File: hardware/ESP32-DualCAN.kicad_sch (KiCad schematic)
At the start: 32 parts, among them J1 Molex 70553 6p, J2 Conn_01x10_Socket, J3 Conn_01x10_Socket, J4 holes, J5 pads, J6 holes, J7 pads, U1 LV2862Y, U2 ESP32-C6-SuperMini, U3 TCAN1044AV, U4 TCAN1044AV, U5 ESP32-C6-Zero, U6 ESP32-C6-SuperMini

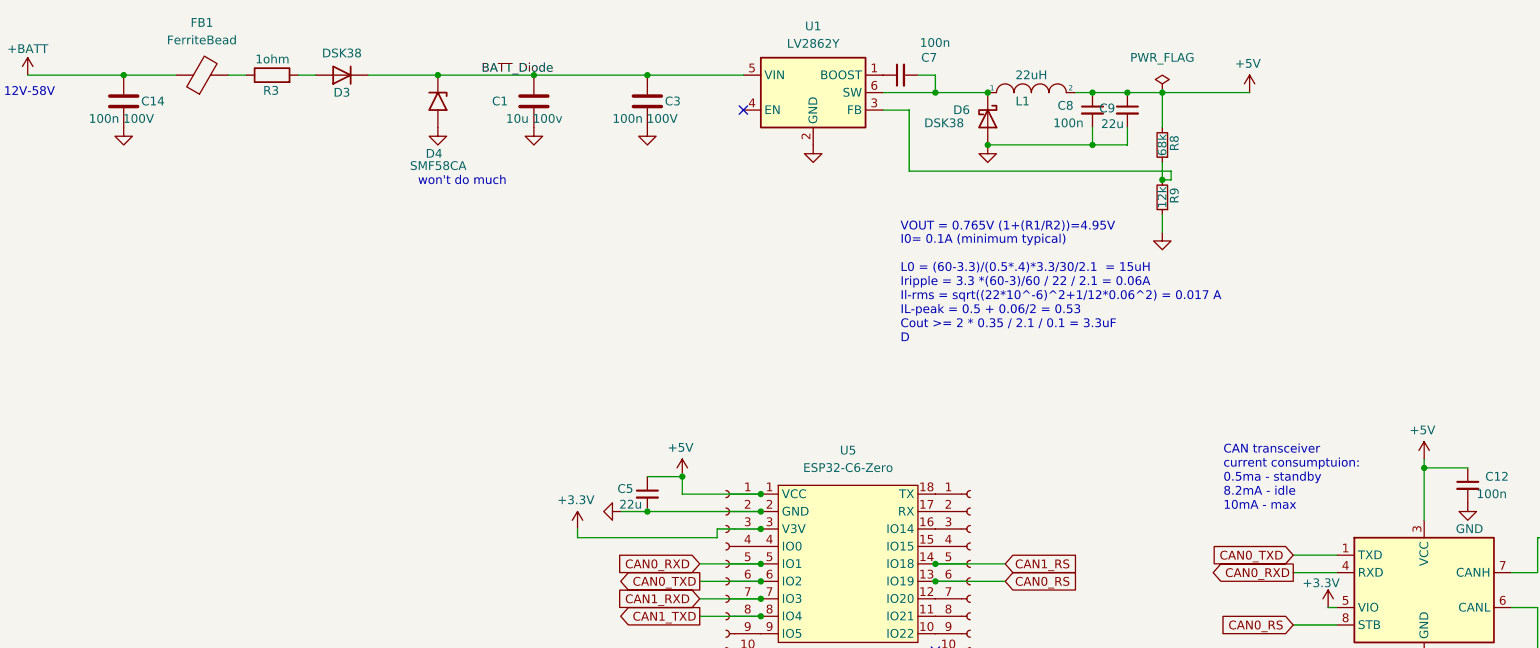
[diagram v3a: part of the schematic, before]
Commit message: DNP input filtering.  Changed vout resistors
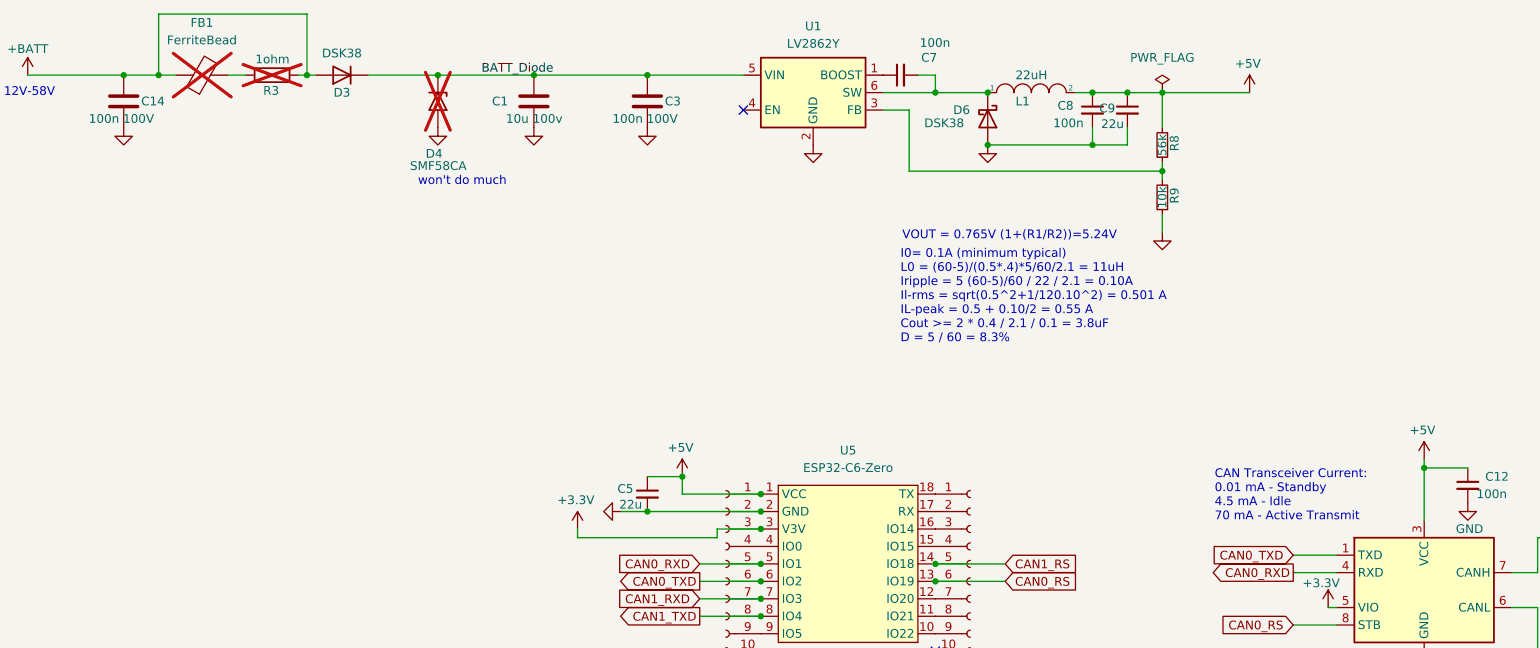
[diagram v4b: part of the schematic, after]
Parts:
- D4, FB1, R3: now not fitted
- J1: LCSC C24361 -> C704582
- R8: value 68k -> 56k; LCSC C36871 -> C25744
- R9: value 12k -> 10k; LCSC C25752 -> C25744
- U1: Alternative LMR51606YF -> LV2862Y, LMR16006Y, LMR51606YF
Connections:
- net +BATT: now also D3.2 (A), R3.2
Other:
- note added: "CAN Transceiver Current: 0.01 mA - Standby 4.5 mA - Idle 70 mA - Active Transmit"
- note added: "I0= 0.1A (minimum typical) L0 = (60-5)/(0.5*.4)*5/60/2.1 = 11uH Iripple = 5 (60-5)/60 / 22 / 2.1 = 0.10A Il-rms = sqrt(0.5^2+1/120.10^2) = 0.501 A IL-peak = 0.5 + 0.10/2 = 0.55 A Cout >= 2 * 0.4 / 2.1 / 0.1 = 3.8uF D = 5 / 60 = 8.3%"
- note added: "VOUT = 0.765V (1+(R1/R2))=5.24V"
- note removed: "CAN transceiver current consumptuion: 0.5ma - standby 8.2mA - idle 10mA - max"
- note removed: "I0= 0.1A (minimum typical) L0 = (60-3.3)/(0.5*.4)*3.3/30/2.1 = 15uH Iripple = 3.3 *(60-3)/60 / 22 / 2.1 = 0.06A Il-rms = sqrt((22*10^-6)^2+1/12*0.06^2) = 0.017 A IL-peak = 0.5 + 0.06/2 = 0.53 Cout >= 2 * 0.35 / 2.1 / 0.1 = 3.3uF D"
- note removed: "VOUT = 0.765V (1+(R1/R2))=4.95V"
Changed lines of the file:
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@@
 		)
 	)
-	(text "CAN transceiver\ncurrent consumptuion:\n0.5ma - standby\n8.2mA - idle\n10mA - max\n"
+	(text "CAN Transceiver Current:\n0.01 mA - Standby\n4.5 mA - Idle\n70 mA - Active Transmit\n"
 		(exclude_from_sim no)
-		(at 199.39 87.63 0)
+		(at 198.12 89.154 0)
 		(effects
 			(font
@@
 		)
 	)
-	(text "VOUT = 0.765V (1+(R1/R2))=4.95V"
+	(text "VOUT = 0.765V (1+(R1/R2))=5.24V"
 		(exclude_from_sim no)
-		(at 152.4 46.99 0)
+		(at 152.654 48.26 0)
 		(effects
 			(font
@@
 		)
 	)
-	(text "I0= 0.1A (minimum typical)\n\nL0 = (60-3.3)/(0.5*.4)*3.3/30/2.1  = 15uH\nIripple = 3.3 *(60-3)/60 / 22 / 2.1 = 0.06A\nIl-rms = sqrt((22*10^-6)^2+1/12*0.06^2) = 0.017 A\nIL-peak = 0.5 + 0.06/2 = 0.53\nCout >= 2 * 0.35 / 2.1 / 0.1 = 3.3uF\nD"
+	(text "I0= 0.1A (minimum typical)\nL0 = (60-5)/(0.5*.4)*5/60/2.1 = 11uH\nIripple = 5 (60-5)/60 / 22 / 2.1 = 0.10A\nIl-rms = sqrt(0.5^2+1/120.10^2) = 0.501 A\nIL-peak = 0.5 + 0.10/2 = 0.55 A\nCout >= 2 * 0.4 / 2.1 / 0.1 = 3.8uF\nD = 5 / 60 = 8.3%"
 		(exclude_from_sim no)
 		(at 152.4 63.246 0)
@@
 	)
 	(junction
-		(at 190.5 39.37)
-		(diameter 0)
-		(color 0 0 0 0)
-	)
-	(junction
 		(at 73.66 179.07)
 		(diameter 0)
@@
 	)
 	(junction
+		(at 66.04 24.13)
+		(diameter 0)
+		(color 0 0 0 0)
+	)
+	(junction
 		(at 157.48 95.25)
 		(diameter 0)
@@
 	)
 	(junction
+		(at 44.45 24.13)
+		(diameter 0)
+		(color 0 0 0 0)
+	)
+	(junction
 		(at 256.54 91.44)
 		(diameter 0)
@@
 	)
 	(junction
+		(at 190.5 38.1)
+		(diameter 0)
+		(color 0 0 0 0)
+	)
+	(junction
 		(at 73.66 181.61)
 		(diameter 0)
@@
 	(wire
 		(pts
-			(xy 54.61 24.13) (xy 57.15 24.13)
+			(xy 99.06 24.13) (xy 115.57 24.13)
 		)
 		(stroke
@@
 	(wire
 		(pts
-			(xy 99.06 24.13) (xy 115.57 24.13)
+			(xy 49.53 184.15) (xy 50.8 184.15)
 		)
 		(stroke
@@
 	(wire
 		(pts
-			(xy 49.53 184.15) (xy 50.8 184.15)
+			(xy 228.6 81.28) (xy 228.6 88.9)
 		)
 		(stroke
@@
 	(wire
 		(pts
-			(xy 228.6 81.28) (xy 228.6 88.9)
+			(xy 157.48 24.13) (xy 157.48 26.67)
 		)
 		(stroke
@@
 	(wire
 		(pts
-			(xy 157.48 24.13) (xy 157.48 26.67)
+			(xy 200.66 254) (xy 209.55 254)
 		)
 		(stroke
@@
 	(wire
 		(pts
-			(xy 200.66 254) (xy 209.55 254)
+			(xy 105.41 91.44) (xy 125.73 91.44)
 		)
 		(stroke
@@
 	(wire
 		(pts
-			(xy 105.41 91.44) (xy 125.73 91.44)
+			(xy 156.21 254) (xy 147.32 254)
 		)
 		(stroke
@@
 	(wire
 		(pts
-			(xy 156.21 254) (xy 147.32 254)
+			(xy 190.5 38.1) (xy 190.5 39.37)
 		)
 		(stroke
@@
 	(wire
 		(pts
-			(xy 204.47 241.3) (xy 209.55 241.3)
+			(xy 44.45 15.24) (xy 66.04 15.24)
 		)
 		(stroke
@@
 	(wire
 		(pts
-			(xy 123.19 102.87) (xy 132.08 102.87)
+			(xy 204.47 241.3) (xy 209.55 241.3)
 		)
 		(stroke
@@
 	(wire
 		(pts
-			(xy 228.6 110.49) (xy 228.6 109.22)
+			(xy 123.19 102.87) (xy 132.08 102.87)
 		)
 		(stroke
@@
 	(wire
 		(pts
-			(xy 156.21 251.46) (xy 147.32 251.46)
+			(xy 228.6 110.49) (xy 228.6 109.22)
 		)
 		(stroke
@@
 	(wire
 		(pts
-			(xy 121.92 107.95) (xy 132.08 107.95)
+			(xy 156.21 251.46) (xy 147.32 251.46)
 		)
 		(stroke
@@
 	(wire
 		(pts
-			(xy 191.77 38.1) (xy 191.77 39.37)
+			(xy 121.92 107.95) (xy 132.08 107.95)
 		)
 		(stroke
@@
 	(wire
 		(pts
-			(xy 123.19 95.25) (xy 132.08 95.25)
+			(xy 44.45 15.24) (xy 44.45 24.13)
 		)
 		(stroke
@@
 	(wire
 		(pts
-			(xy 180.34 34.29) (xy 185.42 34.29)
+			(xy 123.19 95.25) (xy 132.08 95.25)
 		)
 		(stroke
@@
 	(wire
 		(pts
-			(xy 209.55 135.89) (xy 215.9 135.89)
+			(xy 180.34 34.29) (xy 185.42 34.29)
 		)
 		(stroke
@@
 	(wire
 		(pts
-			(xy 242.57 133.35) (xy 242.57 138.43)
+			(xy 209.55 135.89) (xy 215.9 135.89)
 		)
 		(stroke
@@
 	(wire
 		(pts
-			(xy 64.77 24.13) (xy 67.31 24.13)
+			(xy 242.57 133.35) (xy 242.57 138.43)
 		)
 		(stroke
@@
 	(wire
 		(pts
-			(xy 190.5 26.67) (xy 203.2 26.67)
+			(xy 64.77 24.13) (xy 66.04 24.13)
 		)
 		(stroke
@@
 	(wire
 		(pts
-			(xy 242.57 151.13) (xy 254 151.13)
+			(xy 190.5 26.67) (xy 203.2 26.67)
 		)
 		(stroke
@@
 	(wire
 		(pts
-			(xy 85.09 24.13) (xy 99.06 24.13)
+			(xy 242.57 151.13) (xy 254 151.13)
 		)
 		(stroke
@@
 	(wire
 		(pts
-			(xy 191.77 39.37) (xy 190.5 39.37)
+			(xy 85.09 24.13) (xy 99.06 24.13)
 		)
 		(stroke
@@
 	(wire
 		(pts
-			(xy 153.67 38.1) (xy 191.77 38.1)
+			(xy 153.67 38.1) (xy 190.5 38.1)
 		)
 		(stroke
@@
 	(wire
 		(pts
-			(xy 39.37 24.13) (xy 46.99 24.13)
+			(xy 39.37 24.13) (xy 44.45 24.13)
 		)
 		(stroke
@@
 	(wire
 		(pts
+			(xy 54.61 24.13) (xy 57.15 24.13)
+		)
+		(stroke
+			(width 0)
+			(type default)
+		)
+	)
+	(wire
+		(pts
 			(xy 123.19 100.33) (xy 132.08 100.33)
 		)
@@
 	(wire
 		(pts
-			(xy 190.5 36.83) (xy 190.5 39.37)
+			(xy 190.5 36.83) (xy 190.5 38.1)
 		)
 		(stroke
@@
 	(wire
 		(pts
+			(xy 66.04 15.24) (xy 66.04 24.13)
+		)
+		(stroke
+			(width 0)
+			(type default)
+		)
+	)
+	(wire
+		(pts
 			(xy 228.6 123.19) (xy 228.6 121.92)
 		)
@@
 	(wire
 		(pts
+			(xy 44.45 24.13) (xy 46.99 24.13)
+		)
+		(stroke
+			(width 0)
+			(type default)
+		)
+	)
+	(wire
+		(pts
 			(xy 256.54 109.22) (xy 267.97 109.22)
 		)
@@
 	(wire
 		(pts
+			(xy 66.04 24.13) (xy 67.31 24.13)
+		)
+		(stroke
+			(width 0)
+			(type default)
+		)
+	)
+	(wire
+		(pts
 			(xy 62.23 184.15) (xy 68.58 184.15)
 		)
@@
 		(in_bom no)
 		(on_board yes)
-		(in_pos_files yes)
+		(in_pos_files no)
 		(dnp no)
 		(property "Reference" "J2"
@@
 			)
 		)
-		(property "LCSC" "C24361"
+		(property "LCSC" "C704582"
 			(at 55.88 184.15 0)
 			(hide yes)
@@
 		(on_board yes)
 		(in_pos_files yes)
-		(dnp no)
+		(dnp yes)
 		(fields_autoplaced yes)
 		(property "Reference" "FB1"
@@
 			)
 		)
-		(property "Value" "68k"
+		(property "Value" "56k"
 			(at 190.5 34.29 90)
 			(show_name no)
@@
 			)
 		)
-		(property "LCSC" "C36871"
+		(property "LCSC" "C25744"
 			(at 187.96 34.29 0)
 			(hide yes)
@@
 		(on_board yes)
 		(in_pos_files yes)
-		(dnp no)
+		(dnp yes)
 		(property "Reference" "R3"
 			(at 61.976 25.654 90)
@@
 			)
 		)
-		(property "Value" "12k"
+		(property "Value" "10k"
 			(at 190.5 41.91 90)
 			(show_name no)
@@
 			)
 		)
-		(property "LCSC" "C25752"
+		(property "LCSC" "C25744"
 			(at 187.96 41.91 0)
 			(hide yes)
@@
 			)
 		)
-		(property "Alternative" "LMR51606YF"
+		(property "Alternative" "LV2862Y, LMR16006Y, LMR51606YF"
 			(at 139.7 26.67 0)
 			(hide yes)
@@
 		(on_board yes)
 		(in_pos_files yes)
-		(dnp no)
+		(dnp yes)
 		(property "Reference" "D4"
 			(at 83.312 35.56 90)
@@
 		(in_bom no)
 		(on_board yes)
-		(in_pos_files yes)
+		(in_pos_files no)
 		(dnp no)
 		(property "Reference" "J3"

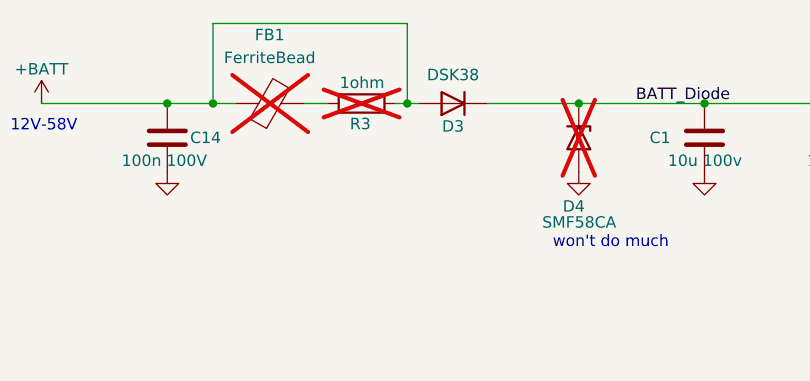
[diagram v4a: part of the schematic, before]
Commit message: cheaper parts, tooling holes
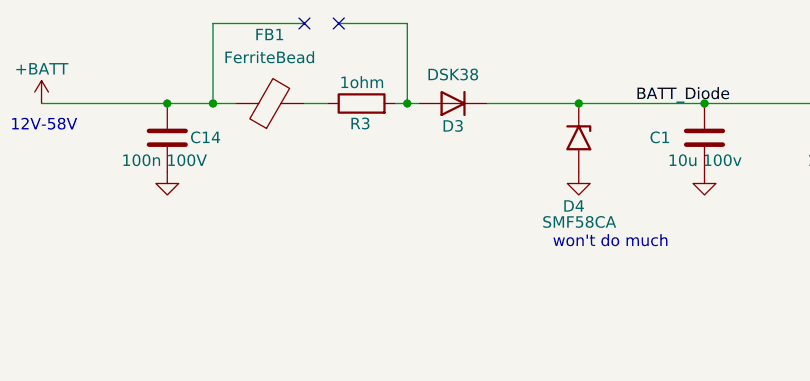
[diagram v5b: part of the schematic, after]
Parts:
- C1: LCSC C576517 -> C5156756
- D4, FB1: now fitted
- R3: LCSC (none) -> C25271; LCSC Part # C25271 -> (none); now fitted
- U1: LCSC C3193152 -> C42403103
- U3: Alternative (none) -> TCAN1044V without extended ESD certification; LCSC C3234993 -> C1852061
- U4: LCSC C3234993 -> C1852061
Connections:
- net +BATT: no longer D3.2 (A), R3.2
- new net: D3.2 (A), R3.2
- no-connect marks 2 -> 4
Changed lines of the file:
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@@
 		(at 129.54 29.21)
 	)
+	(no_connect
+		(at 54.61 15.24)
+	)
+	(no_connect
+		(at 58.42 15.24)
+	)
 	(wire
 		(pts
@@
 	(wire
 		(pts
+			(xy 58.42 15.24) (xy 66.04 15.24)
+		)
+		(stroke
+			(width 0)
+			(type default)
+		)
+	)
+	(wire
+		(pts
 			(xy 99.06 24.13) (xy 115.57 24.13)
 		)
@@
 	(wire
 		(pts
-			(xy 44.45 15.24) (xy 66.04 15.24)
-		)
-		(stroke
-			(width 0)
-			(type default)
-		)
-	)
-	(wire
-		(pts
 			(xy 204.47 241.3) (xy 209.55 241.3)
 		)
@@
 	(wire
 		(pts
+			(xy 44.45 15.24) (xy 54.61 15.24)
+		)
+		(stroke
+			(width 0)
+			(type default)
+		)
+	)
+	(wire
+		(pts
 			(xy 242.57 133.35) (xy 254 133.35)
 		)
@@
 			)
 		)
-		(property "LCSC" "C3234993"
+		(property "LCSC" "C1852061"
 			(at 233.68 111.76 0)
 			(hide yes)
@@
 			)
 		)
+		(property "Alternative" "TCAN1044V without extended ESD certification"
+			(at 228.6 99.06 0)
+			(hide yes)
+			(show_name no)
+			(do_not_autoplace no)
+			(effects
+				(font
+					(size 1.27 1.27)
+				)
+			)
+		)
 		(pin "1"
 		)
@@
 			)
 		)
-		(property "LCSC" "C576517"
+		(property "LCSC" "C5156756"
 			(at 93.98 27.94 0)
 			(hide yes)
@@
 		(on_board yes)
 		(in_pos_files yes)
-		(dnp yes)
+		(dnp no)
 		(fields_autoplaced yes)
 		(property "Reference" "FB1"
@@
 		(on_board yes)
 		(in_pos_files yes)
-		(dnp yes)
+		(dnp no)
 		(property "Reference" "R3"
 			(at 61.976 25.654 90)
@@
 			)
 		)
-		(property "LCSC Part #" "C25271"
-			(at 60.96 24.13 0)
+		(property "LCSC" "C25271"
+			(at 60.96 24.13 90)
 			(hide yes)
 			(show_name no)
@@
 			)
 		)
-		(property "LCSC" "C3193152"
+		(property "LCSC" "C42403103"
 			(at 139.7 26.67 0)
 			(hide yes)
@@
 		(on_board yes)
 		(in_pos_files yes)
-		(dnp yes)
+		(dnp no)
 		(property "Reference" "D4"
 			(at 83.312 35.56 90)
@@
 			)
 		)
-		(property "LCSC" "C3234993"
+		(property "LCSC" "C1852061"
 			(at 233.68 153.67 0)
 			(hide yes)
